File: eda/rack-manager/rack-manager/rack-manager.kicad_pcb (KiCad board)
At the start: 2 copper layers, 95 parts, among them J1 Screw_Terminal_01x02, J10 Screw_Terminal_01x02, J11 Conn_02x03_Odd_Even, J12 Conn_01x02_Pin, J13 Conn_01x04_Socket, J14 Conn_02x06_Counter_Clockwise, J15 Conn_02x06_Counter_Clockwise, J16 Conn_01x04_Socket, J17 Conn_01x04_Socket, J18 Conn_01x04_Socket, J19 Conn_01x04_Socket, J2 Screw_Terminal_01x02, J20 Conn_01x04_Socket, J21 Conn_01x04_Socket, J22 Conn_01x04_Socket, J23 Conn_01x04_Socket, J3 Screw_Terminal_01x02, J4 Screw_Terminal_01x02, J5 Screw_Terminal_01x02, J6 Screw_Terminal_01x02, J7 Screw_Terminal_01x02, J8 Screw_Terminal_01x02, J9 Screw_Terminal_01x02, SW1 SW_Push, U1 ADS131M02IRUKR, U2 ADS131M02IRUKR, U3 ADS131M02IRUKR, U5 TCA9548AMRGER, U6 PCA9555PW

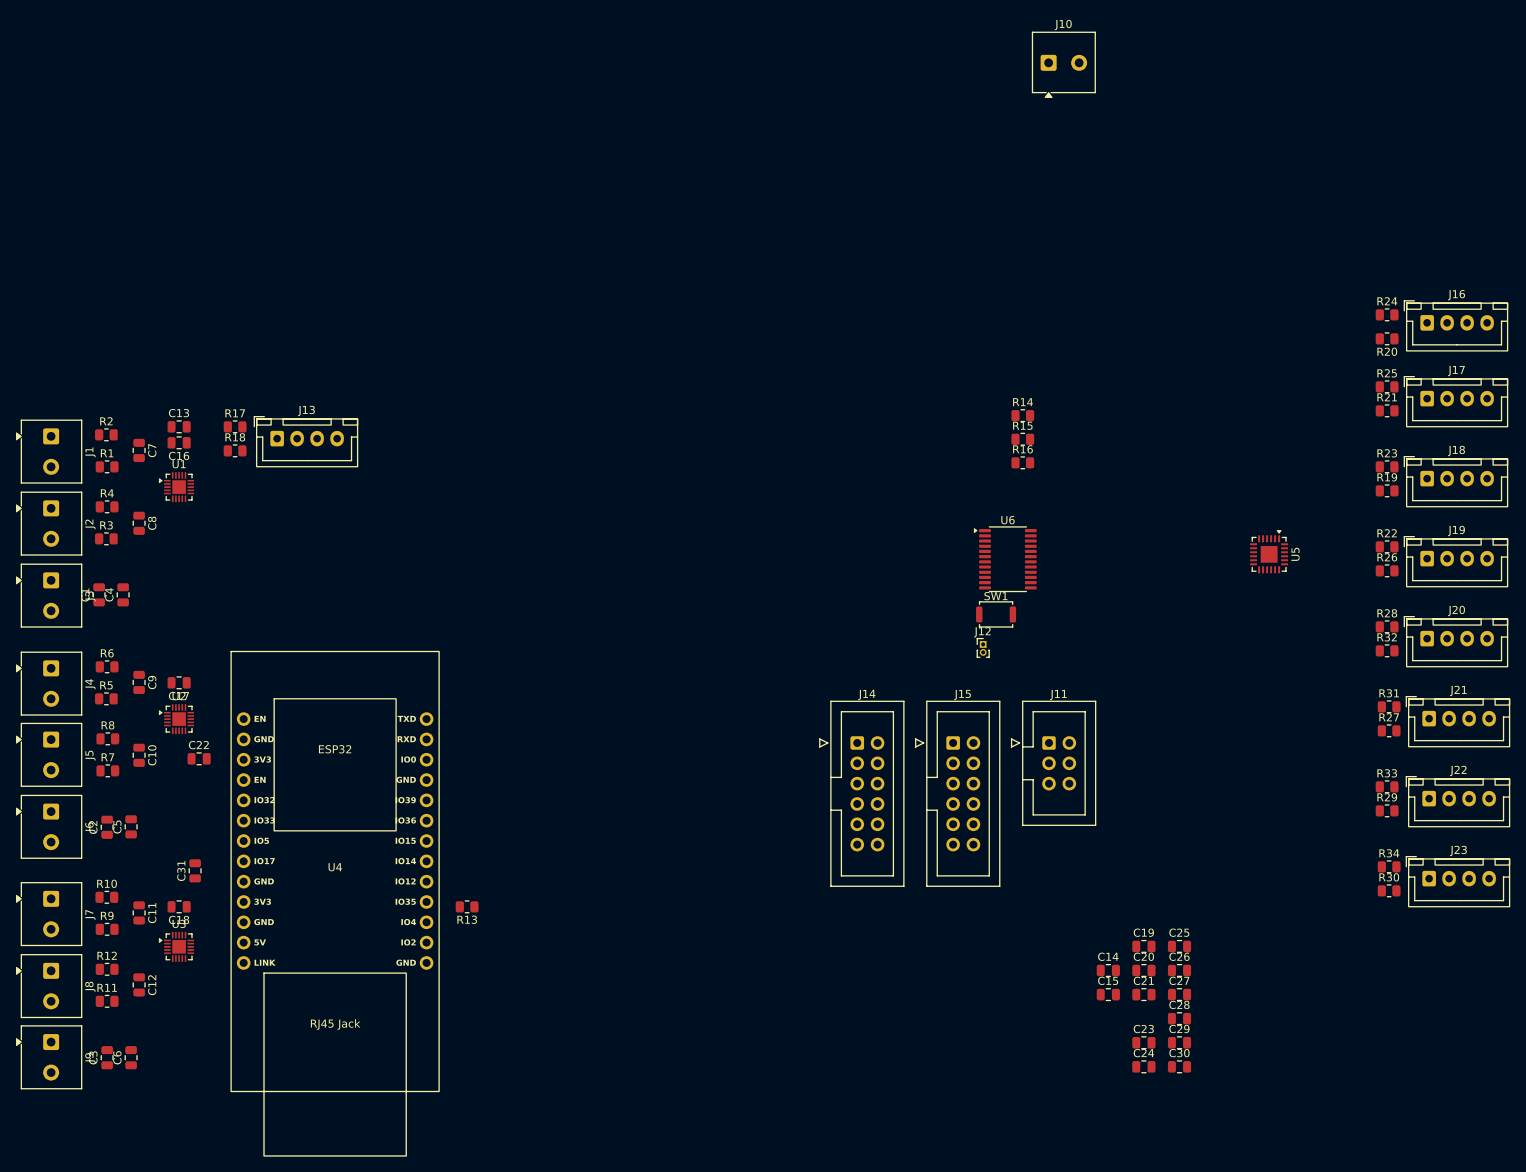
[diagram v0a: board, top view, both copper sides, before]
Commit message: Rack manager PCB component placement
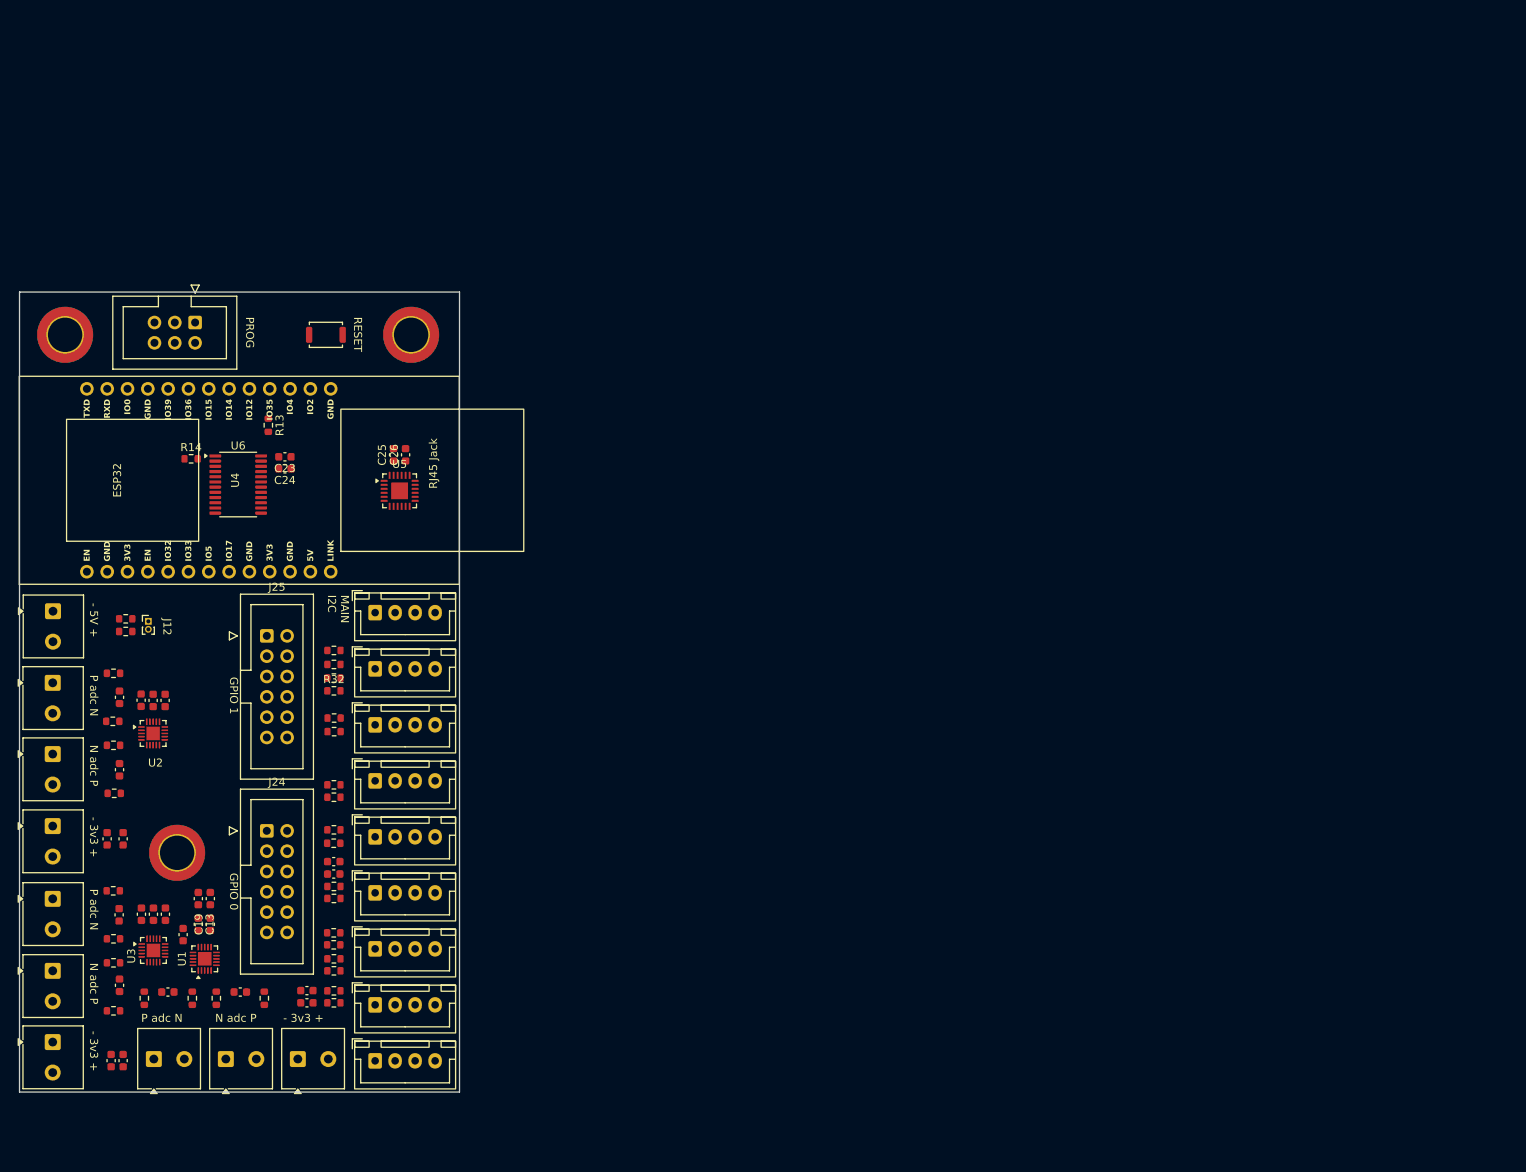
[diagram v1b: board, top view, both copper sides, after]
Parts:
- removed C22, C31: 10uF, Capacitor_SMD:C_0805_2012Metric
- removed J14, J15: Conn_02x06_Counter_Clockwise, Connector_IDC:IDC-Header_2x06_P2.54mm_Vertical
- added H1: MountingHole, MountingHole:MountingHole_4.3mm_M4_ISO14580_Pad_TopBottom, F.Cu at (64.8, 64.5)
- added H2: MountingHole, MountingHole:MountingHole_4.3mm_M4_ISO14580_Pad_TopBottom, F.Cu at (108.0, 64.5)
- added H3: MountingHole, MountingHole:MountingHole_4.3mm_M4_ISO14580_Pad_TopBottom, F.Cu at (78.8, 129.2)
- added J24: Conn_02x06_Odd_Even, Connector_IDC:IDC-Header_2x06_P2.54mm_Vertical, F.Cu at (90.0, 126.5)
- added J25: Conn_02x06_Odd_Even, Connector_IDC:IDC-Header_2x06_P2.54mm_Vertical, F.Cu at (90.0, 102.1)
- C1, C10, C11, C12, C13, C14, C15, C16, C17, C18, C19, C2, C20, C21, C23, C24, C25, C26, C27, C28, C29, C3, C30, C4, C5, C6, C7, C8, C9: footprint Capacitor_SMD:C_0805_2012Metric -> Capacitor_SMD:C_0603_1608Metric
- R1, R10, R11, R12, R13, R14, R15, R16, R17, R18, R19, R2, R20, R21, R22, R23, R24, R25, R26, R27, R28, R29, R3, R30, R31, R32, R33, R34, R4, R5, R6, R7, R8, R9: footprint Resistor_SMD:R_0805_2012Metric -> Resistor_SMD:R_0603_1608Metric
- moved J19 145.7 mm to (103.5, 155.2)
- moved J18 144.0 mm to (103.5, 141.2)
- moved R23 144.0 mm to (98.3, 139.2)
- moved R19 143.4 mm to (98.3, 140.8)
- moved R22 142.9 mm to (98.3, 146.5)
- moved R25 142.8 mm to (98.3, 126.4)
- moved J17 142.5 mm to (103.5, 127.2)
- moved R21 142.3 mm to (98.3, 128.1)
- moved R26 142.3 mm to (98.3, 148.0)
- moved J10 142.1 mm to (63.2, 99.0), turned to -90 degrees
- moved R24 140.9 mm to (98.4, 112.4), turned to 180 degrees
- moved J16 140.8 mm to (103.5, 113.2)
- moved R20 140.5 mm to (98.4, 114.1), turned to 0 degrees
- moved J23 132.7 mm to (103.5, 148.2)
- moved R34 132.4 mm to (98.3, 142.5)
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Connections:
- J11 pad 1: +3V3 -> GND
- J11 pad 2: GND -> +3V3
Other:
- board outline added: 55 x 100 mm
- copper layers 2 -> 4
- board text added: "- 3v3 +"
- board text added: "- 5V +"
- board text added: "GPIO 0"
- board text added: "GPIO 1"
- board text added: "I2C 0"
- board text added: "I2C 1"
- board text added: "I2C 2"
- board text added: "I2C 3"
- board text added: "I2C 4"
- board text added: "I2C 5"
- board text added: "I2C 6"
- board text added: "I2C 7"
- board text added: "MAIN I2C"
- board text added: "N adc P"
- board text added: "P adc N"
- board text added: "PROG"
- board text added: "RESET"

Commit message: Rack monitoring board routing
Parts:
- moved R14 13.7 mm to (92.5, 86.7), turned to 180 degrees
- moved C23 12.8 mm to (80.6, 85.1)
- moved C24 12.8 mm to (80.6, 86.6)
- moved SW1 5.55 mm to (91.8, 64.3), turned to -90 degrees
- moved R18 3.30 mm to (98.3, 102.4)
- moved R31 2.15 mm to (98.4, 120.2)
- moved R23 1.65 mm to (98.3, 140.9)
- moved R34 1.60 mm to (98.3, 144.1)
- moved R32 1.60 mm to (98.3, 107.4)
- moved R28 1.50 mm to (98.3, 108.9)
- moved R30 1.40 mm to (98.3, 142.6)
- moved R19 1.35 mm to (98.3, 139.4)
- moved R16 0.98 mm to (72.3, 100.6)
- moved R15 0.98 mm to (72.3, 99.0)
- moved R27 0.95 mm to (98.4, 121.7)
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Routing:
- net Net-(J11-Pin_3): track 0.00 -> 70.2 mm
- net /I2C.SDA7: track 0.00 -> 11.6 mm
- net Net-(J11-Pin_4): track 0.00 -> 10.9 mm
- net Net-(J11-Pin_6): track 0.00 -> 10.8 mm
- net Net-(J11-Pin_5): track 0.00 -> 9.69 mm
- net /I2C.SDA6: track 0.00 -> 9.22 mm
- net /I2C.SCL7: track 0.00 -> 9.06 mm
- net Net-(J13-Pin_2): track 0.00 -> 8.78 mm
- net Net-(U3-AIN1P): track 0.00 -> 8.39 mm
- net Net-(U1-AIN1P): track 0.00 -> 8.34 mm
- net Net-(U2-AIN1P): track 0.00 -> 8.22 mm
- net Net-(U3-AIN0P): track 0.00 -> 7.96 mm
- net /I2C.SDA0: track 0.00 -> 7.92 mm
- net Net-(U2-AIN0P): track 0.00 -> 7.92 mm
- net Net-(J2-Pin_2): track 0.00 -> 7.87 mm
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
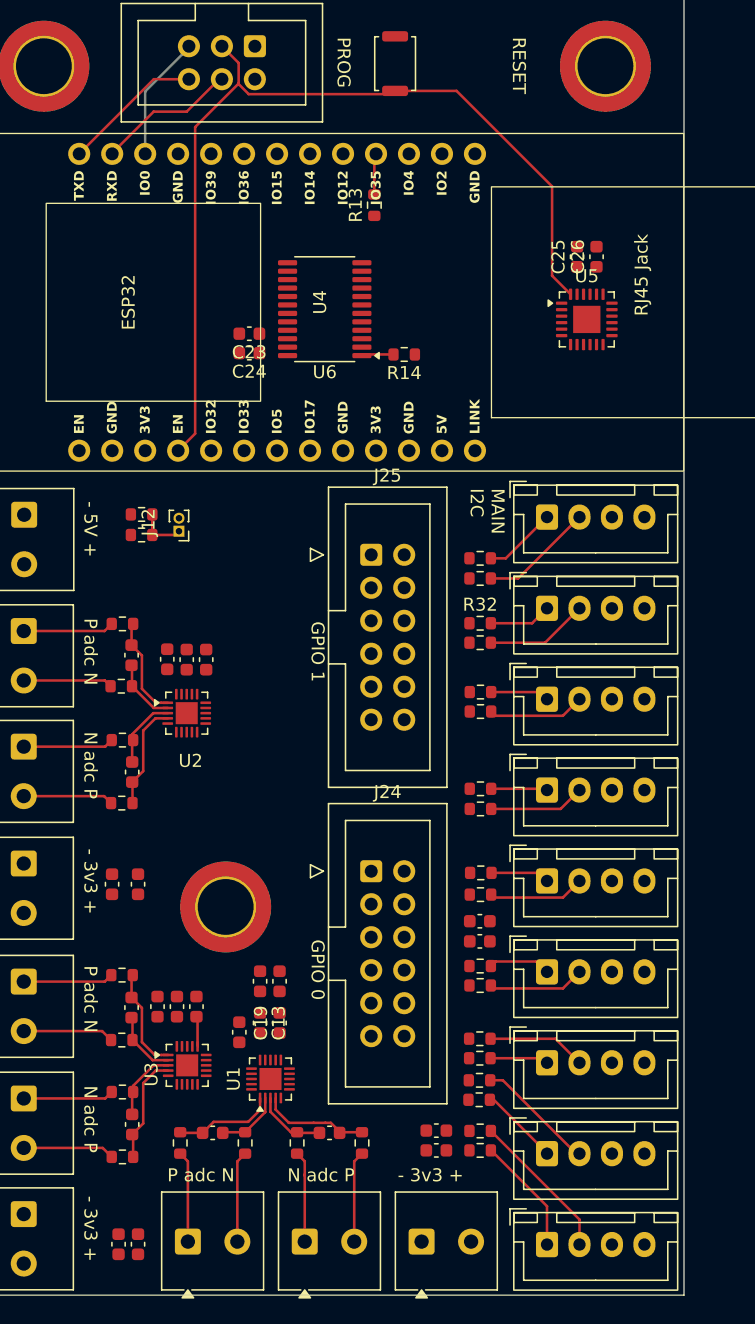
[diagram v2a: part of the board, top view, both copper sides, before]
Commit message: Rack manager board routing
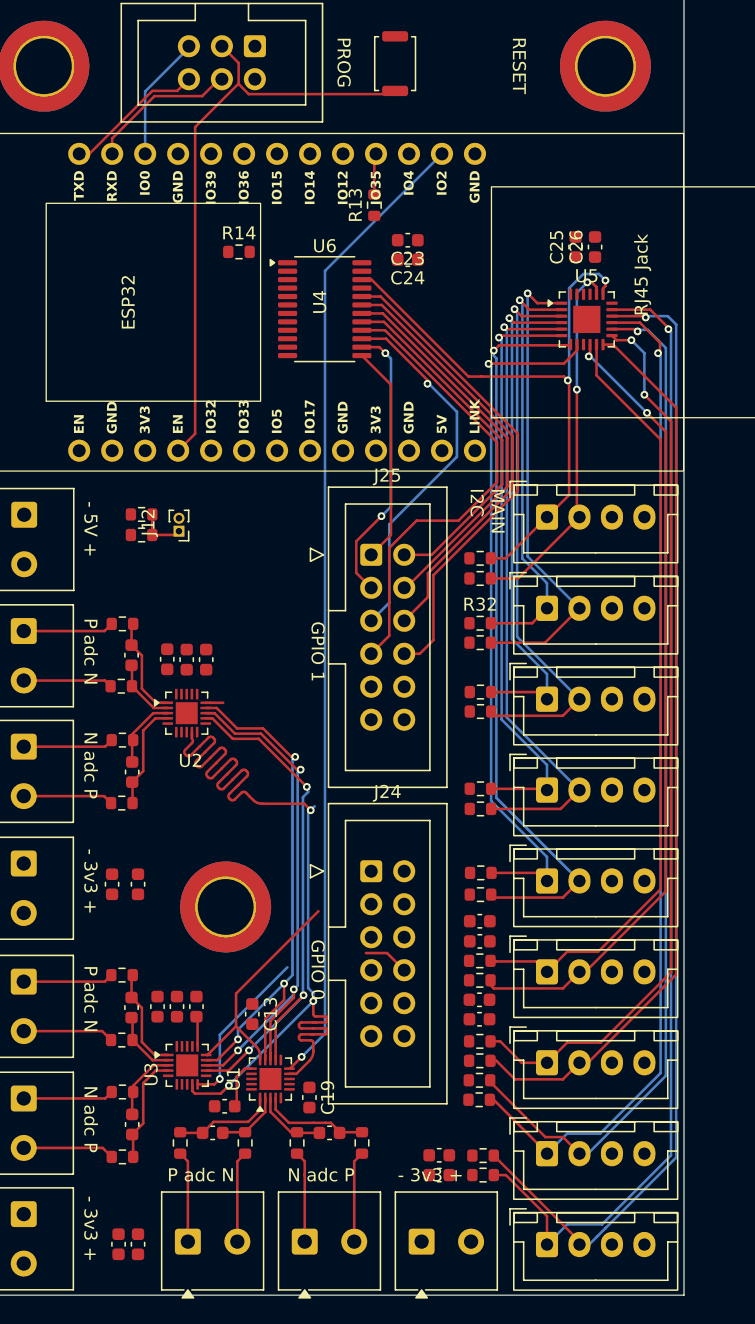
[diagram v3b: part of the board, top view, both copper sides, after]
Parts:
- moved C28 17.2 mm to (98.3, 137.9), turned to 180 degrees
- moved C30 15.5 mm to (98.3, 136.4), turned to 180 degrees
- moved R14 15.0 mm to (79.8, 78.8), turned to 0 degrees
- moved C23 14.2 mm to (92.8, 77.9)
- moved C24 14.2 mm to (92.8, 79.4)
- moved C19 6.18 mm to (85.2, 143.9), turned to -90 degrees
- moved C16 5.81 mm to (78.7, 144.6), turned to 180 degrees
- moved C1 1.91 mm to (95.2, 149.9)
- moved C4 1.91 mm to (95.2, 148.4)
- moved R22 1.91 mm to (98.6, 148.4)
- moved R26 1.91 mm to (98.6, 149.9)
- moved R19 1.70 mm to (98.3, 141.1)
- moved R23 1.30 mm to (98.3, 139.6)
- moved C13 0.91 mm to (80.8, 137.5)
- moved C25 0.76 mm to (105.7, 78.4)
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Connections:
- R13 pad 2: Net-(U1-DRDY) -> Net-(U2-DRDY)
- U1 pad 11: Net-(U1-DRDY) -> unconnected-(U1-DRDY-Pad11)
- U2 pad 11: unconnected-(U2-DRDY-Pad11) -> Net-(U2-DRDY)
- U4 pad 17: Net-(U1-DRDY) -> Net-(U2-DRDY)
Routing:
- net /I2C.SCL7: track 9.06 -> 88.7 mm, vias 0 -> 1
- net /I2C.SDA7: track 11.6 -> 89.3 mm, vias 0 -> 1
- net Net-(U1-CS): track 0.00 -> 75.3 mm, vias 0 -> 1
- net Net-(U1-SYNC/RESET): track 0.00 -> 74.2 mm, vias 0 -> 3
- net /I2C.SCL6: track 6.15 -> 78.2 mm, vias 0 -> 1
- net /I2C.SDA6: track 9.22 -> 79.3 mm, vias 0 -> 1
- net /I2C.SCL5: track 4.49 -> 69.1 mm, vias 0 -> 2
- net /I2C.SDA5: track 7.62 -> 69.5 mm
- net /I2C.SCL4: track 4.80 -> 60.1 mm
- net /I2C.SDA4: track 7.45 -> 61.8 mm, vias 0 -> 2
- net /I2C.SDA3: track 7.42 -> 57.1 mm, vias 0 -> 1
- net /I2C.SCL3: track 4.53 -> 53.9 mm, vias 0 -> 1
- net /I2C.SDA2: track 7.40 -> 49.9 mm, vias 0 -> 1
- net Net-(J13-Pin_1): track 5.64 -> 47.8 mm, vias 0 -> 2
- net Net-(U1-SCLK): track 0.00 -> 42.1 mm, vias 0 -> 3
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
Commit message: Finished routing
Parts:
- moved R16 42.6 mm to (91.8, 62.7), turned to -90 degrees
- moved R15 42.0 mm to (93.4, 62.7), turned to -90 degrees
- moved J12 38.6 mm to (92.1, 65.6), turned to 90 degrees
- moved SW1 8.90 mm to (100.7, 64.2)
- moved R14 7.80 mm to (87.5, 77.7), turned to 180 degrees
- moved R13 2.12 mm to (88.1, 74.9), turned to 135 degrees
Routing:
- net Net-(U1-CLKIN): track 19.4 -> 117.0 mm, vias 0 -> 4
- net Net-(U1-SCLK): track 42.1 -> 118.5 mm
- net Net-(U2-CS): track 0.00 -> 67.2 mm, vias 0 -> 1
- net /GPIO07: track 3.50 -> 69.3 mm, vias 0 -> 2
- net /GPIO03: track 0.00 -> 55.4 mm, vias 0 -> 2
- net Net-(U1-SYNC/RESET): track 74.2 -> 129.0 mm, vias 3 -> 4
- net /GPIO02: track 0.00 -> 53.4 mm
- net /GPIO06: track 0.00 -> 52.1 mm, vias 0 -> 2
- net Net-(U1-DOUT): track 41.8 -> 93.9 mm, vias 3 -> 4
- net Net-(U2-DRDY): track 3.18 -> 54.5 mm, vias 0 -> 4
- net /GPIO01: track 0.00 -> 50.7 mm, vias 0 -> 2
- net /GPIO05: track 0.00 -> 49.2 mm
- net /GPIO04: track 0.00 -> 49.1 mm
- net /GPIO00: track 0.00 -> 48.6 mm, vias 0 -> 2
- net Net-(U3-CS): track 12.6 -> 53.2 mm
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
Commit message: More routing
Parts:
- J12: footprint Connector_PinHeader_1.00mm:PinHeader_1x02_P1.00mm_Vertical -> Connector_PinHeader_2.54mm:PinHeader_1x02_P2.54mm_Vertical
- moved C1 2.27 mm to (94.0, 148.0)
- moved C4 2.27 mm to (94.0, 146.5)
- moved R22 2.27 mm to (97.3, 146.5)
- moved R26 2.27 mm to (97.3, 148.0)
- moved C3 2.18 mm to (68.4, 154.6)
- moved C6 2.18 mm to (69.9, 154.6)
- moved C16 2.08 mm to (76.6, 144.5)
- moved C15 1.30 mm to (74.6, 137.6)
- moved C18 1.30 mm to (77.6, 137.6)
- moved C21 1.30 mm to (76.1, 137.6)
- moved C19 0.97 mm to (85.5, 143.0)
- moved R15 0.64 mm to (93.4, 62.1)
- moved R16 0.64 mm to (91.8, 62.1)
- moved C14 0.49 mm to (74.5, 110.6)
- moved C17 0.49 mm to (77.5, 110.6)
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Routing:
- net +5V: track 0.00 -> 131.5 mm
- net +3V3: track 0.00 -> 38.2 mm, vias 0 -> 14
- net GND: track 0.00 -> 9.25 mm, vias 0 -> 5
- net Net-(U1-DOUT): track 93.9 -> 87.7 mm
- net Net-(J11-Pin_3): track 82.5 -> 85.3 mm, vias 3 -> 4
- net Net-(U1-AIN1N): track 5.51 -> 7.70 mm
- net Net-(U1-AIN0N): track 5.03 -> 7.14 mm
- net Net-(U3-AIN1N): track 5.58 -> 7.69 mm
- net Net-(U2-AIN1N): track 5.55 -> 7.60 mm
- net Net-(U3-AIN0N): track 5.15 -> 7.15 mm
- net Net-(U2-AIN0N): track 5.07 -> 7.01 mm
- net /I2C.SCL7: track 88.7 -> 90.2 mm
- net /I2C.SDA6: track 79.3 -> 77.9 mm
- net Net-(U1-CAP): track 3.73 -> 5.15 mm
- net /I2C.SCL6: track 78.2 -> 77.2 mm
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- added copper zone on In2.Cu, net +3V3
- added copper zone on In1.Cu, net GND
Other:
- board text added: "Jonn 2026"
- board text added: "[VAULT]"

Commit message: Silkscreen
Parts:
- added G***: LOGO, LOGO, B.Cu at (74.2, 143.1)
- SW1: value SW_Push -> C720477
- moved C3 3.50 mm to (71.9, 154.7), turned to -90 degrees
- moved C29 1.60 mm to (98.3, 130.3), turned to 180 degrees
- moved C1 1.53 mm to (93.9, 146.5), turned to 0 degrees
- moved C4 1.53 mm to (93.9, 148.0), turned to 0 degrees
- moved C27 1.50 mm to (98.3, 131.8), turned to 180 degrees
- moved H3 1.27 mm to (77.5, 129.5)
- moved C6 0.51 mm to (70.4, 154.7), turned to -90 degrees
- moved H2 0.50 mm to (108.5, 64.5)
- moved C21 0.32 mm to (76.1, 137.3)
- moved H1 0.25 mm to (64.5, 64.5)
- renumbered U2 to ADC1, U3 to ADC2, U1 to ADC3
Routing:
- net +3V3: track 38.2 -> 106.1 mm, vias 14 -> 29
- net GND: track 9.25 -> 69.4 mm, vias 5 -> 24
- net Net-(J13-Pin_1): track 72.3 -> 69.3 mm
- net Net-(J13-Pin_2): track 66.5 -> 67.6 mm, vias 3 -> 4
- net Net-(ADC1-CAP): track 1.86 -> 2.81 mm
- added copper zone on F.Cu, net +3V3
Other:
- board text added: "1"
- board text added: "2"
- board text added: "3"
- board text added: "3V3"
- board text added: "5V"
- board text added: "A"
- board text added: "ADC CLKIN"
- board text added: "ADC DIN"
- board text added: "ADC DRDY"
- board text added: "ADC SCLK"
- board text added: "ADC SYNC"
- board text added: "ADC1 CS"
- board text added: "ADC1 DOUT"
- board text added: "ADC2 CS"
- board text added: "ADC3 CS"
- board text added: "B"
- board text added: "EN"
- board text added: "ETH LINK"
- board text added: "GND"
- board text added: "IO0"
- board text added: "IO12"
- board text added: "IO14"
- board text added: "IO15"
- board text added: "IO17"
- board text added: "IO2"
- board text added: "IO32"
- board text added: "IO33"
- board text added: "IO35"
- board text added: "IO36"
- board text added: "IO39"
- board text added: "IO4"
- board text added: "IO5"
- board text added: "LINK"
- board text added: "N P"
- board text added: "P N"
- board text added: "R13"
- board text added: "RXD"
- board text added: "TXD"
- board text added: "v0.1"
- board text removed: "N adc P"
- board text removed: "P adc N"

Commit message: Final PCB design, work on 3D cad files
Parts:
- added C22: 200uF, Capacitor_THT:CP_Radial_D8.0mm_P3.50mm, F.Cu at (74.9, 102.7)
- moved R16 7.18 mm to (88.4, 68.4), turned to 0 degrees
- moved R15 6.89 mm to (88.4, 66.8), turned to 0 degrees
- moved J12 1.82 mm to (91.8, 67.4)
- moved R13 1.44 mm to (87.5, 76.2), turned to 180 degrees
- moved SW1 1.30 mm to (102.0, 64.2)
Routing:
- net +5V: track 131.5 -> 141.6 mm
- net Net-(J11-Pin_3): track 85.3 -> 87.7 mm, vias 4 -> 3
- net Net-(ADC1-DRDY): track 54.5 -> 55.4 mm
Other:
- board text added: "3v3"
- board text added: "ETH"
- board text added: "IO1"
- board text added: "IO3"
- board text removed: "ETH LINK"
